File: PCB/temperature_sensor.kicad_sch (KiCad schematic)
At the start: 8 parts, among them Q3 FDS6690A, U8 MCP9700T-ETT

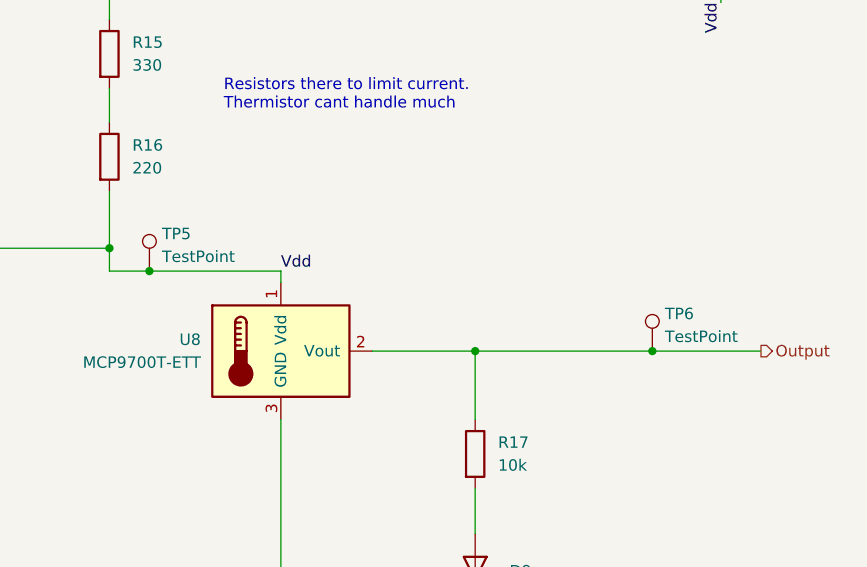
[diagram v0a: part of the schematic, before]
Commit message: Labelled Test Points
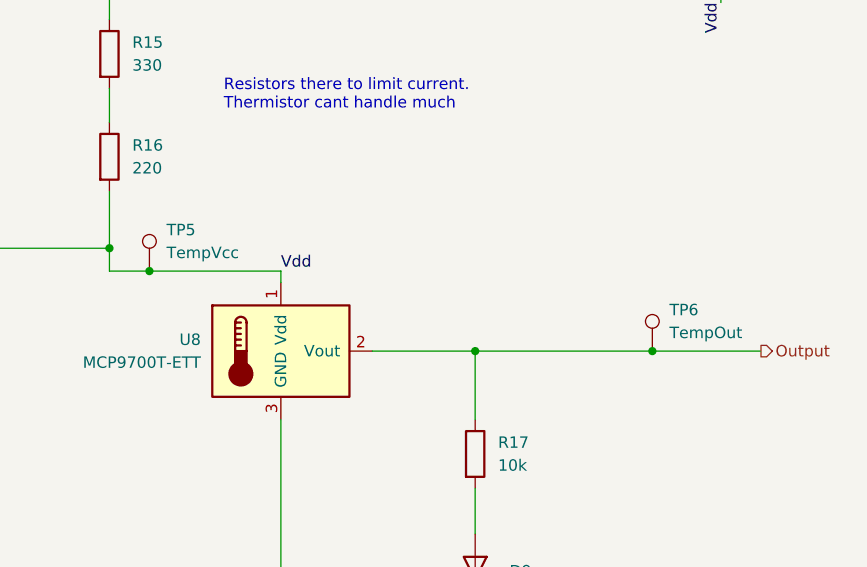
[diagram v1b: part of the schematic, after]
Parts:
- TP5: value TestPoint -> TempVcc
- TP6: value TestPoint -> TempOut
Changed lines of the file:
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@@
   (symbol (lib_id "Connector:TestPoint") (at 150.495 66.04 0) (unit 1)
     (in_bom yes) (on_board yes) (fields_autoplaced)
-    (property "Reference" "TP5" (id 0) (at 151.892 61.9033 0)
+    (property "Reference" "TP5" (id 0) (at 152.4 61.4679 0)
       (effects (font (size 1.27 1.27)) (justify left))
     )
-    (property "Value" "TestPoint" (id 1) (at 151.892 64.4402 0)
+    (property "Value" "TempVcc" (id 1) (at 152.4 64.0079 0)
       (effects (font (size 1.27 1.27)) (justify left))
     )
@@
   (symbol (lib_id "Connector:TestPoint") (at 206.375 74.93 0) (unit 1)
     (in_bom yes) (on_board yes) (fields_autoplaced)
-    (property "Reference" "TP6" (id 0) (at 207.772 70.7933 0)
+    (property "Reference" "TP6" (id 0) (at 208.28 70.3579 0)
       (effects (font (size 1.27 1.27)) (justify left))
     )
-    (property "Value" "TestPoint" (id 1) (at 207.772 73.3302 0)
+    (property "Value" "TempOut" (id 1) (at 208.28 72.8979 0)
       (effects (font (size 1.27 1.27)) (justify left))
     )

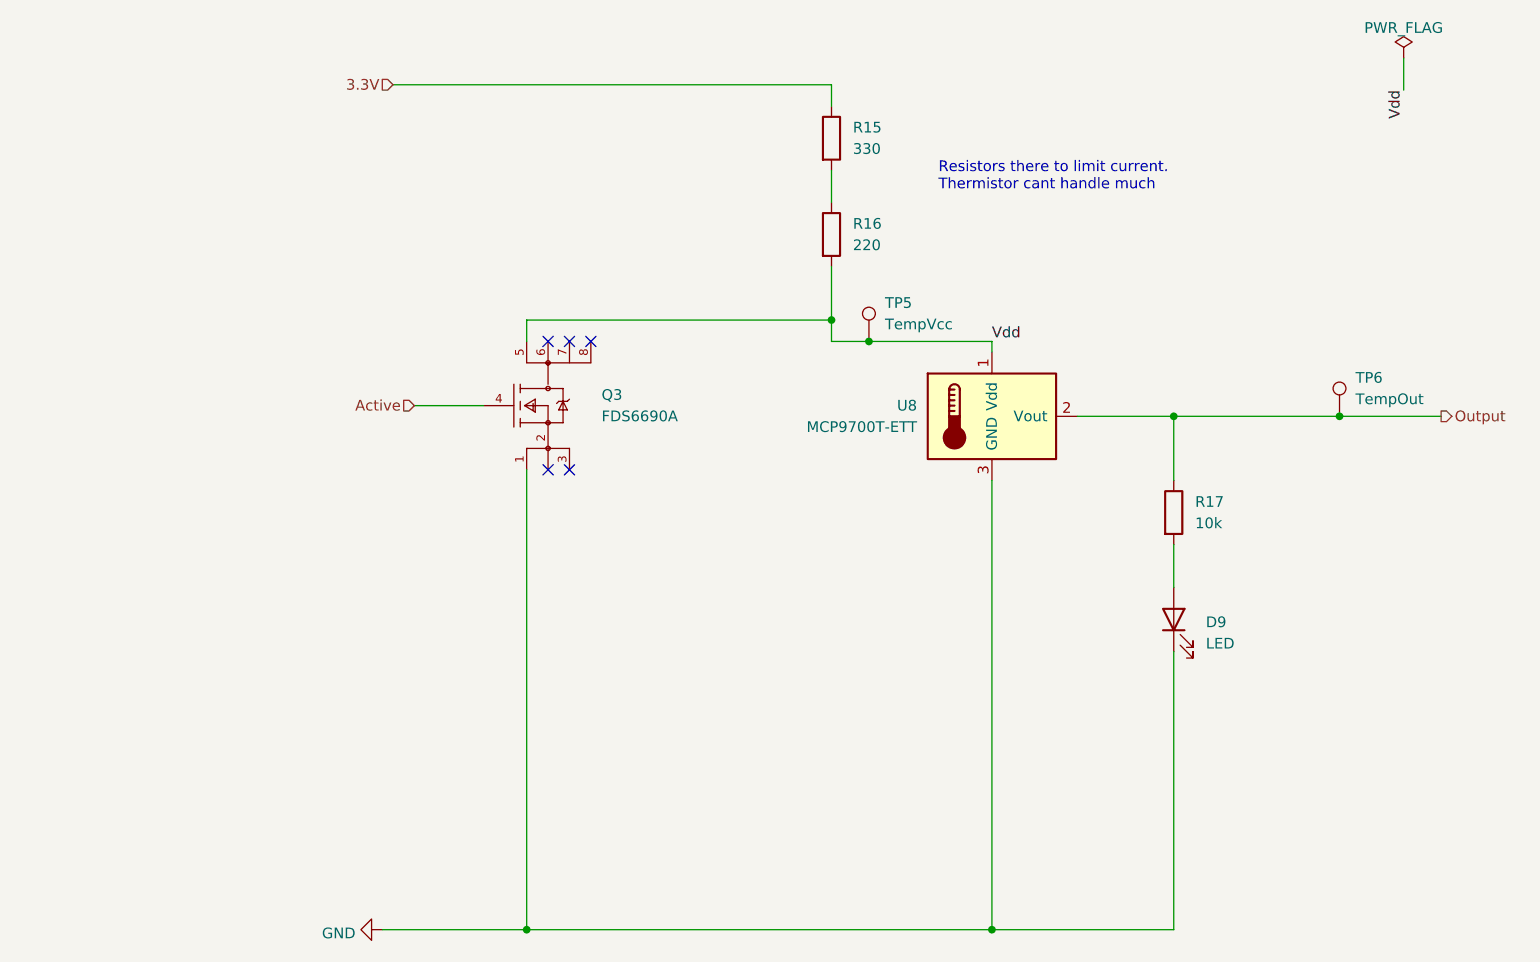
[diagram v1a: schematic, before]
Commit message: Mostly addressed issues with Sensing subsystem
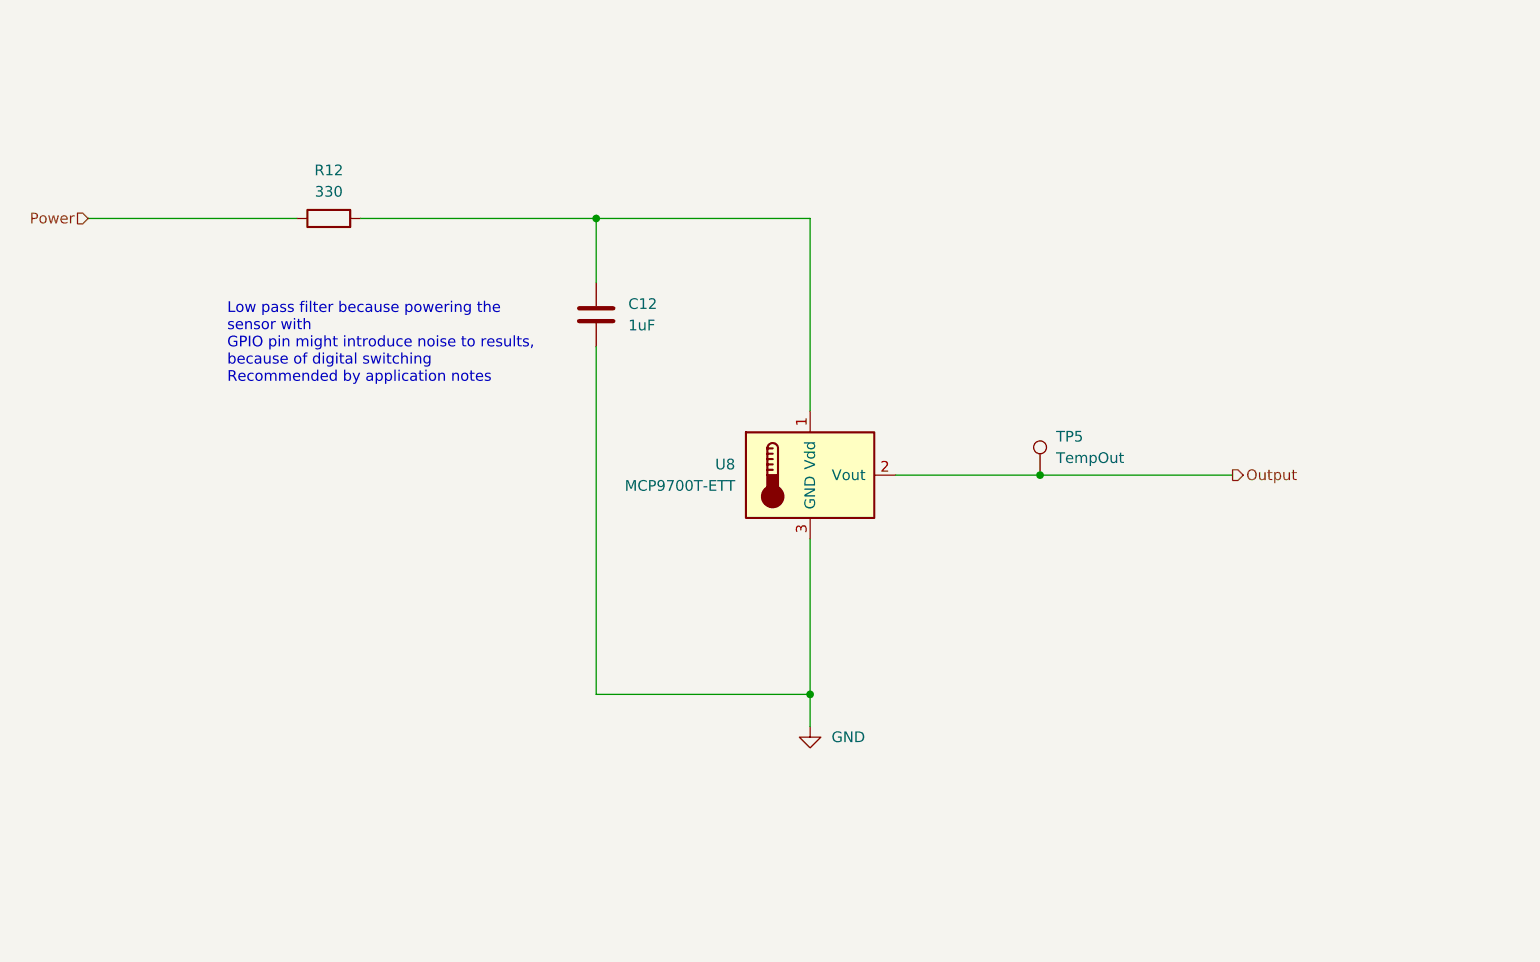
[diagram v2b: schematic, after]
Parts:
- removed D9: LED, LED_SMD:LED_0603_1608Metric, symbol Device:LED
- removed Q3: FDS6690A, Package_SO:SOIC-8_3.9x4.9mm_P1.27mm, symbol Symbol_EEE3088F:FDS6690A
- removed R15: 330, Resistor_SMD:R_0402_1005Metric, symbol Device:R
- removed R16: 220, Resistor_SMD:R_0402_1005Metric, symbol Device:R
- removed R17: 10k, Resistor_SMD:R_0402_1005Metric, symbol Device:R
- removed TP6: TempOut, TestPoint:TestPoint_Pad_D1.0mm, symbol Connector:TestPoint
- added C12: 1uF, Capacitor_SMD:CP_Elec_5x5.3, symbol Device:C
- added R12: 330, Resistor_SMD:R_0402_1005Metric, symbol Device:R
- TP5: value TempVcc -> TempOut
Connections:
- net GND: now also C12.2
- net Output: now also TP5.1
- net Vdd: no longer names the net of U8.1 (Vdd)
- net Vdd: now also C12.1, R12.2; no longer TP5.1
- new net Power: R12.1
- no-connect marks 5 -> 0
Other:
- note added: "Low pass filter because powering the sensor with GPIO pin might introduce noise to results, because of digital switching Recommended by application notes"
- note removed: "Resistors there to limit current. Thermistor cant handle much"

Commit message: Prepare PCB
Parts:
- C12: footprint Capacitor_SMD:CP_Elec_5x5.3 -> Capacitor_SMD:C_0402_1005Metric; JLC Part # C72491 -> C52923; LCSC (none) -> C52923
- R12: JLC Part # C25104 -> C25104; LCSC (none) -> C25104
- U8: LCSC (none) -> C42288
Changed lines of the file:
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@@
       (effects (font (size 1.27 1.27)) (justify left))
     )
-    (property "Footprint" "Capacitor_SMD:CP_Elec_5x5.3" (id 2) (at 119.0752 66.675 0)
+    (property "Footprint" "Capacitor_SMD:C_0402_1005Metric" (id 2) (at 119.0752 66.675 0)
       (effects (font (size 1.27 1.27)) hide)
     )
@@
       (effects (font (size 1.27 1.27)) hide)
     )
-    (property "JLC Part #" "C72491" (id 5) (at 118.11 62.865 0)
+    (property "JLC Part #" "C52923" (id 5) (at 118.11 62.865 0)
+      (effects (font (size 1.27 1.27)) hide)
+    )
+    (property "LCSC" "C52923" (id 6) (at 118.11 62.865 0)
       (effects (font (size 1.27 1.27)) hide)
     )
@@
       (effects (font (size 1.27 1.27)) hide)
     )
-    (property "JLC Part #" " C25104" (id 5) (at 86.36 51.435 0)
+    (property "JLC Part #" "C25104" (id 5) (at 86.36 51.435 0)
       (effects (font (size 1.27 1.27)) hide)
     )
     (property "Price" "0.0007" (id 6) (at 86.36 51.435 0)
+      (effects (font (size 1.27 1.27)) hide)
+    )
+    (property "LCSC" "C25104" (id 7) (at 86.36 51.435 0)
       (effects (font (size 1.27 1.27)) hide)
     )
@@
       (effects (font (size 1.27 1.27)) hide)
     )
+    (property "LCSC" "C42288" (id 7) (at 143.51 81.915 0)
+      (effects (font (size 1.27 1.27)) hide)
+    )
